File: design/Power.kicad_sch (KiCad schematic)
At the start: 48 parts, among them U2 TC2117, U3 DRV8302

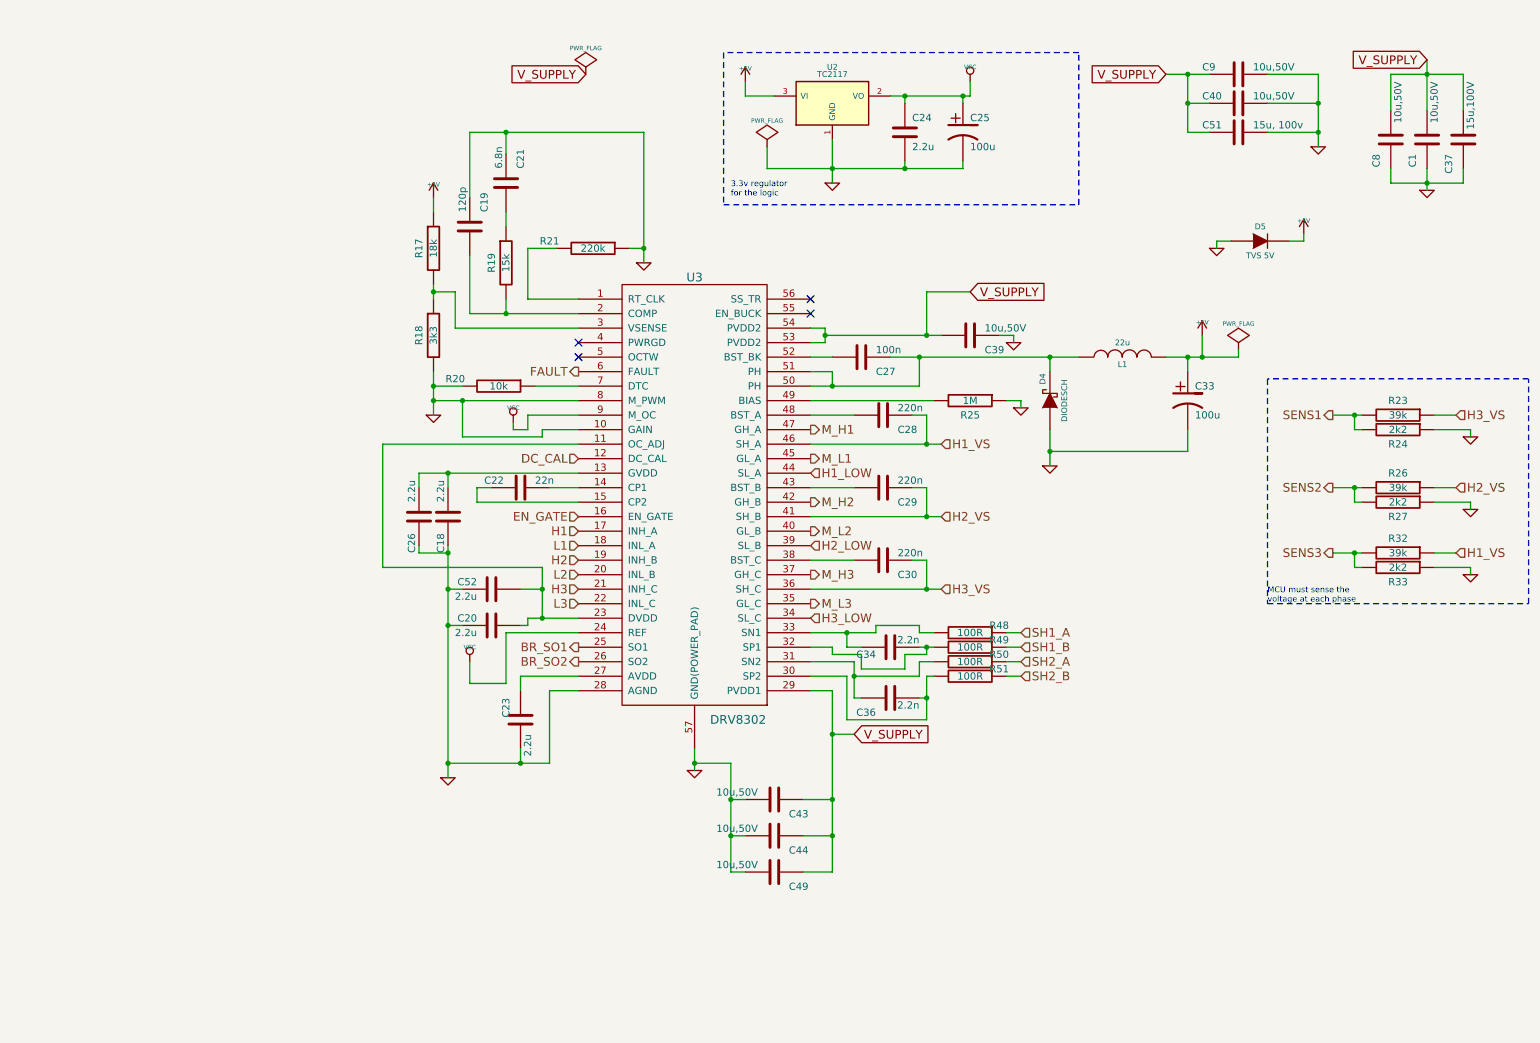
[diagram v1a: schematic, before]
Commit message: Actualización VESC6.4
Actualización a esquemáticos de VESC6.4, faltan asignación de huellas y descripción a cada elemento.
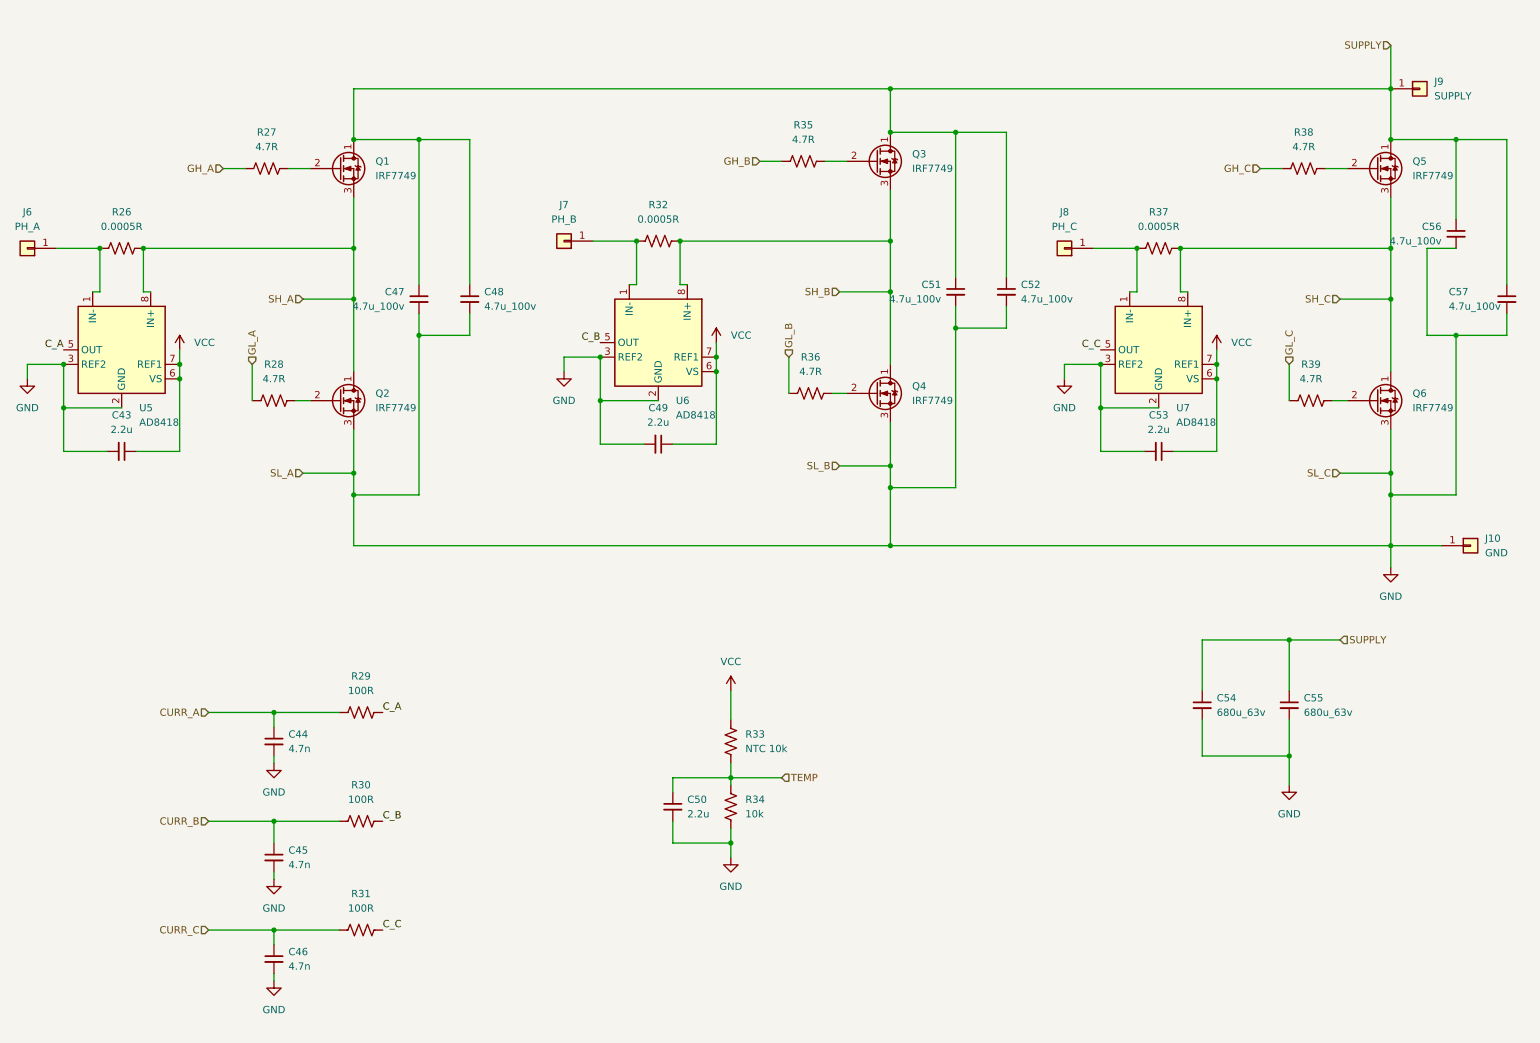
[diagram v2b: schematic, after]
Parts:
- removed C1, C39, C40, C43, C44, C49, C8, C9: 10u,50V, CRF1:SMD-1206, symbol BLDC_4-rescue1:C-RESCUE-BLDC_4
- removed C18, C20, C23, C24, C26, C52: 2.2u, CRF1:SMD-0603_c, symbol BLDC_4-rescue1:C-RESCUE-BLDC_4
- removed C19: 120p, CRF1:SMD-0603_c, symbol BLDC_4-rescue1:C-RESCUE-BLDC_4
- removed C21: 6.8n, CRF1:SMD-0603_c, symbol BLDC_4-rescue1:C-RESCUE-BLDC_4
- removed C22: 22n, CRF1:SMD-0603_c, symbol BLDC_4-rescue1:C-RESCUE-BLDC_4
- removed C25, C33: 100u, w_smd_cap:c_tant_B, symbol BLDC_4-rescue1:CP1-RESCUE-BLDC_4
- removed C27: 100n, CRF1:SMD-0603_c, symbol BLDC_4-rescue1:C-RESCUE-BLDC_4
- removed C28, C29, C30: 220n, CRF1:SMD-0603_c, symbol BLDC_4-rescue1:C-RESCUE-BLDC_4
- removed C34, C36: 2.2n, CRF1:SMD-0603_c, symbol BLDC_4-rescue1:C-RESCUE-BLDC_4
- removed C37: 15u,100V, w_smd_cap:c_2220, symbol BLDC_4-rescue1:C-RESCUE-BLDC_4
- removed C51: 15u, 100v, w_smd_cap:c_2220, symbol BLDC_4-rescue1:C-RESCUE-BLDC_4
- removed D4: DIODESCH, Diodes_SMD:SMA_Handsoldering, symbol BLDC_4-rescue1:DIODESCH
- removed D5: TVS 5V, w_smd_diode:do214ac, symbol BLDC_4-rescue1:DIODE
- removed L1: 22u, w_smd_inductors:inductor_smd_8x5mm, symbol BLDC_4-rescue1:INDUCTOR
- removed R17: 18k, CRF1:SMD-0603_r, symbol BLDC_4-rescue1:R-RESCUE-BLDC_4
- removed R18: 3k3, CRF1:SMD-0603_r, symbol BLDC_4-rescue1:R-RESCUE-BLDC_4
- removed R19: 15k, CRF1:SMD-0603_r, symbol BLDC_4-rescue1:R-RESCUE-BLDC_4
- removed R20: 10k, CRF1:SMD-0603_r, symbol BLDC_4-rescue1:R-RESCUE-BLDC_4
- removed R21: 220k, CRF1:SMD-0603_r, symbol BLDC_4-rescue1:R-RESCUE-BLDC_4
- removed R23, R26, R32: 39k, CRF1:SMD-0603_r, symbol BLDC_4-rescue1:R-RESCUE-BLDC_4
- removed R24, R27, R33: 2k2, CRF1:SMD-0603_r, symbol BLDC_4-rescue1:R-RESCUE-BLDC_4
- removed R25: 1M, CRF1:SMD-0603_r, symbol BLDC_4-rescue1:R-RESCUE-BLDC_4
- removed R48, R49, R50, R51: 100R, CRF1:SMD-0603_r, symbol BLDC_4-rescue1:R-RESCUE-BLDC_4
- removed U2: TC2117, CRF1:SOT-223, symbol BLDC_4-rescue1:NCP1117ST33T3G
- removed U3: DRV8302, CRF1:TSSOP-56-PP, symbol crf_11:DRV8302
- added C43, C49, C50, C53: 2.2u, Capacitor_SMD:C_0603_1608Metric, symbol Device:C_Small
- added C44, C45, C46: 4.7n, Capacitor_SMD:C_0603_1608Metric, symbol Device:C_Small
- added C47, C48, C51, C52, C56, C57: 4.7u_100v, Capacitor_SMD:C_0603_1608Metric, symbol Device:C_Small
- added C54, C55: 680u_63v, Capacitor_SMD:C_0603_1608Metric, symbol Device:C_Small
- added J10: GND, symbol Connector_Generic:Conn_01x01
- added J6: PH_A, symbol Connector_Generic:Conn_01x01
- added J7: PH_B, symbol Connector_Generic:Conn_01x01
- added J8: PH_C, symbol Connector_Generic:Conn_01x01
- added J9: SUPPLY, symbol Connector_Generic:Conn_01x01
- added Q1, Q2, Q3, Q4, Q5, Q6: IRF7749, Package_DirectFET:DirectFET_L8, symbol bldc:IRF7749L1PBF
- added R26, R32, R37: 0.0005R, Resistor_SMD:R_0603_1608Metric, symbol Device:R_US
- added R27, R28, R35, R36, R38, R39: 4.7R, Resistor_SMD:R_0603_1608Metric, symbol Device:R_US
- added R29, R30, R31: 100R, Resistor_SMD:R_0603_1608Metric, symbol Device:R_US
- added R33: NTC 10k, Resistor_SMD:R_0603_1608Metric, symbol Device:R_US
- added R34: 10k, Resistor_SMD:R_0603_1608Metric, symbol Device:R_US
- added U5, U6, U7: AD8418, symbol Amplifier_Current:AD8418
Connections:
- net GND: now also C43.2, C44.2, C45.2, C46.2, C47.2, C48.2, C49.2, C50.2, C51.2, C52.2, C53.2, C54.2, C55.2, C56.2, C57.2, J10.1 (Pin_1), Q2.3 (S), Q4.3 (S), Q6.3 (S), R34.2, U5.2 (GND), U5.3 (REF2), U6.2 (GND), U6.3 (REF2), U7.2 (GND), U7.3 (REF2)
- net VCC: now also C43.1, C49.1, C53.1, R33.1, U5.6 (VS), U5.7 (REF1), U6.6 (VS), U6.7 (REF1), U7.6 (VS), U7.7 (REF1)
- new net: Q3.2 (G), R35.1
- new net: J7.1 (Pin_1), R32.2, U6.1 (IN-)
- new net: Q4.2 (G), R36.1
- new net: J6.1 (Pin_1), R26.2, U5.1 (IN-)
- new net: Q1.2 (G), R27.1
- new net: Q2.2 (G), R28.1
- new net: J8.1 (Pin_1), R37.2, U7.1 (IN-)
- new net: Q5.2 (G), R38.1
- new net: Q6.2 (G), R39.1
- new net CURR_A: C44.1, R29.2
- new net CURR_B: C45.1, R30.2
- new net CURR_C: C46.1, R31.2
- new net C_A: R29.1, U5.5 (OUT)
- new net C_B: R30.1, U6.5 (OUT)
- new net C_C: R31.1, U7.5 (OUT)
- new net GH_A: R27.2
- new net GH_B: R35.2
- new net GH_C: R38.2
- new net GL_A: R28.2
- new net GL_B: R36.2
- new net GL_C: R39.2
- new net SH_A: Q1.3 (S), Q2.1 (D), R26.1, U5.8 (IN+)
- new net SH_B: Q3.3 (S), Q4.1 (D), R32.1, U6.8 (IN+)
- new net SH_C: Q5.3 (S), Q6.1 (D), R37.1, U7.8 (IN+)
- new net SUPPLY: C47.1, C48.1, C51.1, C52.1, C54.1, C55.1, C56.1, C57.1, J9.1 (Pin_1), Q1.1 (D), Q3.1 (D), Q5.1 (D)
- new net TEMP: C50.1, R33.2, R34.1
- no-connect marks 4 -> 0
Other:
- note removed: "3.3v regulator for the logic"
- note removed: "MCU must sense the voltage at each phase"
- company: Benjamin Vedder -> UTN
- title: BLDC Driver 4.11 -> bldc-controller-edp

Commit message: Impresión de esquemático en pdf
Impresión de la versión del esquemático en la carpeta /pdf
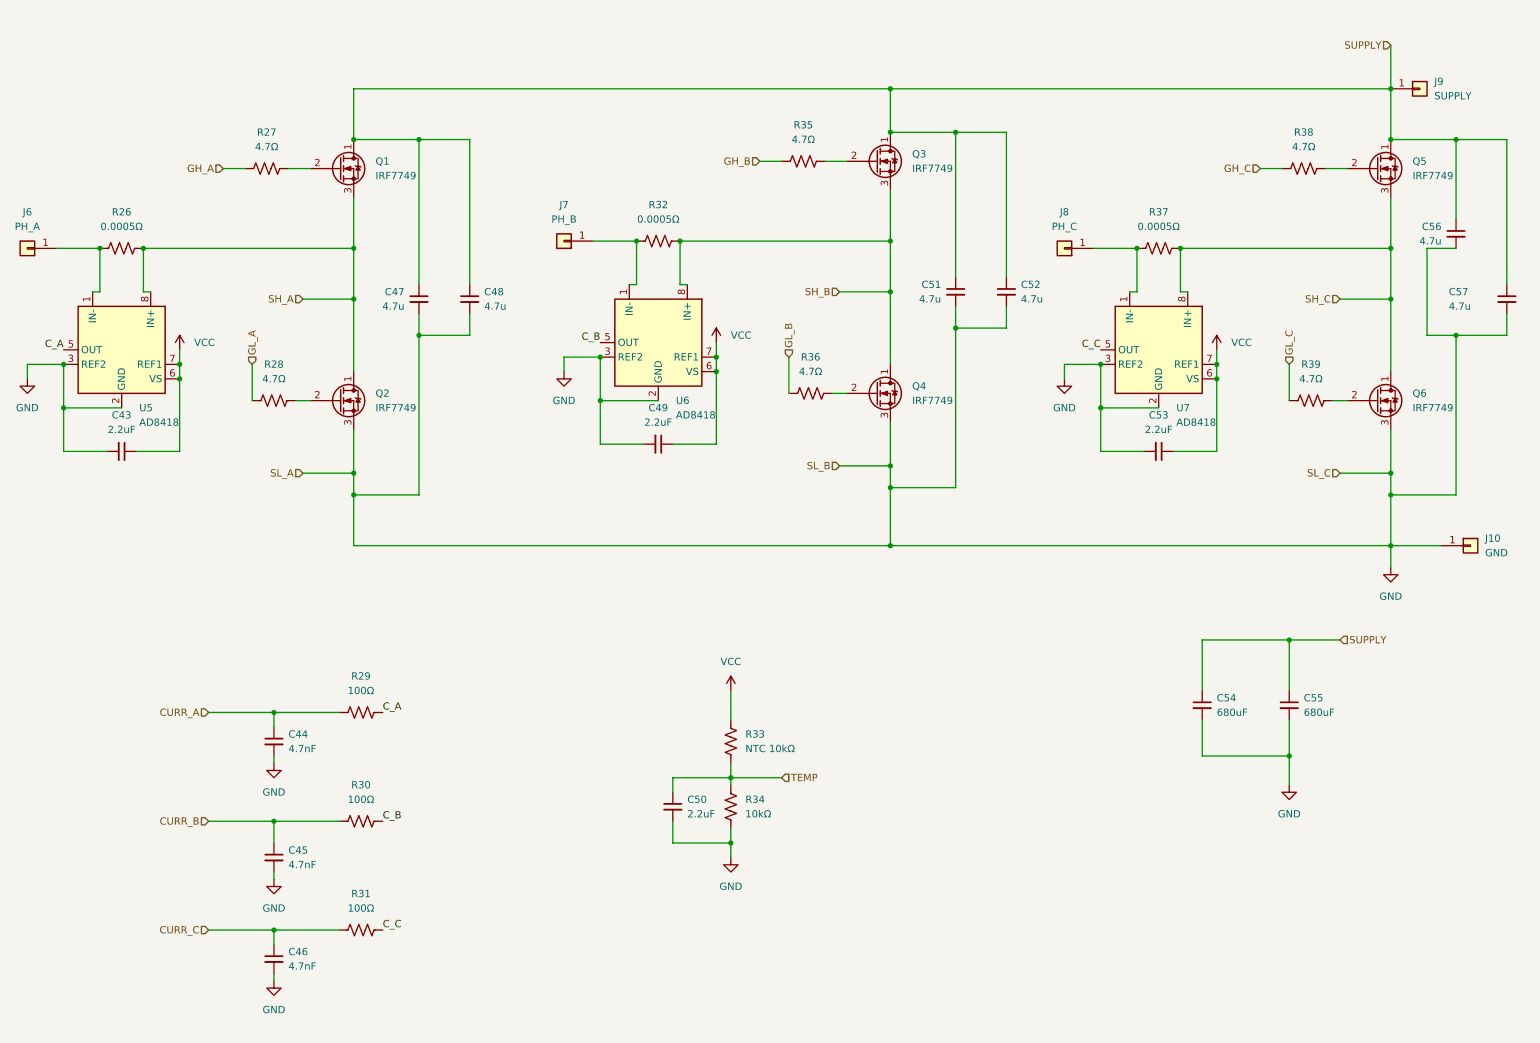
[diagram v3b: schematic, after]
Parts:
- C43, C49, C50, C53: value 2.2u -> 2.2uF
- C44, C45, C46: value 4.7n -> 4.7nF
- C47, C48, C51, C52, C56, C57: value 4.7u_100v -> 4.7u; footprint Capacitor_SMD:C_0603_1608Metric -> Capacitor_SMD:C_1210_3225Metric
- C54, C55: value 680u_63v -> 680uF; footprint Capacitor_SMD:C_0603_1608Metric -> Capacitor_THT:CP_Radial_D6.3mm_P2.50mm
- R26, R32, R37: value 0.0005R -> 0.0005Ω
- R27, R28, R35, R36, R38, R39: value 4.7R -> 4.7Ω
- R29, R30, R31: value 100R -> 100Ω
- R33: value NTC 10k -> NTC 10kΩ
- R34: value 10k -> 10kΩ
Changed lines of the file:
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@@
 			)
 		)
-		(property "Value" "4.7R"
+		(property "Value" "4.7Ω"
 			(at 154.94 36.83 90)
 			(effects
@@
 			)
 		)
-		(property "Value" "0.0005R"
+		(property "Value" "0.0005Ω"
 			(at 129.54 50.8 90)
 			(effects
@@
 			)
 		)
-		(property "Value" "4.7R"
+		(property "Value" "4.7Ω"
 			(at 156.21 77.47 90)
 			(effects
@@
 			)
 		)
-		(property "Value" "4.7u_100v"
+		(property "Value" "4.7u"
 			(at 179.07 64.7762 0)
 			(effects
@@
 			)
 		)
-		(property "Footprint" "Capacitor_SMD:C_0603_1608Metric"
+		(property "Footprint" "Capacitor_SMD:C_1210_3225Metric"
 			(at 181.61 63.5 0)
 			(effects
@@
 			)
 		)
-		(property "Description" ""
+		(property "Description" "CAP CER 4.7UF 100V X7R 1210"
 			(at 181.61 63.5 0)
 			(effects
@@
 			)
 		)
-		(property "Value" "4.7u_100v"
+		(property "Value" "4.7u"
 			(at 193.04 64.7762 0)
 			(effects
@@
 			)
 		)
-		(property "Footprint" "Capacitor_SMD:C_0603_1608Metric"
+		(property "Footprint" "Capacitor_SMD:C_1210_3225Metric"
 			(at 190.5 63.5 0)
 			(effects
@@
 			)
 		)
-		(property "Description" ""
+		(property "Description" "CAP CER 4.7UF 100V X7R 1210"
 			(at 190.5 63.5 0)
 			(effects
@@
 			)
 		)
-		(property "Value" "2.2u"
+		(property "Value" "2.2uF"
 			(at 129.5336 86.36 90)
 			(effects
@@
 			)
 		)
-		(property "Value" "4.7R"
+		(property "Value" "4.7Ω"
 			(at 60.96 38.1 90)
 			(effects
@@
 			)
 		)
-		(property "Value" "0.0005R"
+		(property "Value" "0.0005Ω"
 			(at 35.56 52.07 90)
 			(effects
@@
 			)
 		)
-		(property "Value" "4.7R"
+		(property "Value" "4.7Ω"
 			(at 62.23 78.74 90)
 			(effects
@@
 			)
 		)
-		(property "Value" "4.7u_100v"
+		(property "Value" "4.7u"
 			(at 85.09 66.0462 0)
 			(effects
@@
 			)
 		)
-		(property "Footprint" "Capacitor_SMD:C_0603_1608Metric"
+		(property "Footprint" "Capacitor_SMD:C_1210_3225Metric"
 			(at 87.63 64.77 0)
 			(effects
@@
 			)
 		)
-		(property "Description" ""
+		(property "Description" "CAP CER 4.7UF 100V X7R 1210"
 			(at 87.63 64.77 0)
 			(effects
@@
 			)
 		)
-		(property "Value" "4.7u_100v"
+		(property "Value" "4.7u"
 			(at 99.06 66.0462 0)
 			(effects
@@
 			)
 		)
-		(property "Footprint" "Capacitor_SMD:C_0603_1608Metric"
+		(property "Footprint" "Capacitor_SMD:C_1210_3225Metric"
 			(at 96.52 64.77 0)
 			(effects
@@
 			)
 		)
-		(property "Description" ""
+		(property "Description" "CAP CER 4.7UF 100V X7R 1210"
 			(at 96.52 64.77 0)
 			(effects
@@
 			)
 		)
-		(property "Value" "2.2u"
+		(property "Value" "2.2uF"
 			(at 35.5536 87.63 90)
 			(effects
@@
 			)
 		)
-		(property "Value" "4.7R"
+		(property "Value" "4.7Ω"
 			(at 242.57 38.1 90)
 			(effects
@@
 			)
 		)
-		(property "Value" "0.0005R"
+		(property "Value" "0.0005Ω"
 			(at 217.17 52.07 90)
 			(effects
@@
 			)
 		)
-		(property "Value" "4.7R"
+		(property "Value" "4.7Ω"
 			(at 243.84 78.74 90)
 			(effects
@@
 			)
 		)
-		(property "Value" "4.7u_100v"
+		(property "Value" "4.7u"
 			(at 266.7 54.6162 0)
 			(effects
@@
 			)
 		)
-		(property "Footprint" "Capacitor_SMD:C_0603_1608Metric"
+		(property "Footprint" "Capacitor_SMD:C_1210_3225Metric"
 			(at 269.24 53.34 0)
 			(effects
@@
 			)
 		)
-		(property "Description" ""
+		(property "Description" "CAP CER 4.7UF 100V X7R 1210"
 			(at 269.24 53.34 0)
 			(effects
@@
 			)
 		)
-		(property "Value" "4.7u_100v"
+		(property "Value" "4.7u"
 			(at 267.97 66.04 0)
 			(effects
@@
 			)
 		)
-		(property "Footprint" "Capacitor_SMD:C_0603_1608Metric"
+		(property "Footprint" "Capacitor_SMD:C_1210_3225Metric"
 			(at 278.13 64.77 0)
 			(effects
@@
 			)
 		)
-		(property "Description" ""
+		(property "Description" "CAP CER 4.7UF 100V X7R 1210"
 			(at 278.13 64.77 0)
 			(effects
@@
 			)
 		)
-		(property "Value" "2.2u"
+		(property "Value" "2.2uF"
 			(at 217.1636 87.63 90)
 			(effects
@@
 			)
 		)
-		(property "Value" "100R"
+		(property "Value" "100Ω"
 			(at 77.47 133.35 90)
 			(effects
@@
 			)
 		)
-		(property "Value" "100R"
+		(property "Value" "100Ω"
 			(at 77.47 152.4 90)
 			(effects
@@
 			)
 		)
-		(property "Value" "100R"
+		(property "Value" "100Ω"
 			(at 77.47 171.45 90)
 			(effects
@@
 			)
 		)
-		(property "Value" "4.7n"
+		(property "Value" "4.7nF"
 			(at 64.77 143.5162 0)
 			(effects
@@
 			)
 		)
-		(property "Description" ""
+		(property "Description" "CAP CER 0603 4.7NF 16V X7R 10%"
 			(at 62.23 142.24 0)
 			(effects
@@
 			)
 		)
-		(property "Value" "4.7n"
+		(property "Value" "4.7nF"
 			(at 64.77 163.8362 0)
 			(effects
@@
 			)
 		)
-		(property "Description" ""
+		(property "Description" "CAP CER 0603 4.7NF 16V X7R 10%"
 			(at 62.23 162.56 0)
 			(effects
@@
 			)
 		)
-		(property "Value" "4.7n"
+		(property "Value" "4.7nF"
 			(at 64.77 181.6162 0)
 			(effects
@@
 			)
 		)
-		(property "Description" ""
+		(property "Description" "CAP CER 0603 4.7NF 16V X7R 10%"
 			(at 62.23 180.34 0)
 			(effects
@@
 			)
 		)
-		(property "Value" "10k"
+		(property "Value" "10kΩ"
 			(at 144.78 154.9399 0)
 			(effects
@@
 			)
 		)
-		(property "Value" "NTC 10k"
+		(property "Value" "NTC 10kΩ"
 			(at 144.78 143.5099 0)
 			(effects
@@
 			)
 		)
-		(property "Value" "2.2u"
+		(property "Value" "2.2uF"
 			(at 134.62 154.9462 0)
 			(effects
@@
 			)
 		)
-		(property "Value" "680u_63v"
+		(property "Value" "680uF"
 			(at 227.33 137.1662 0)
 			(effects
@@
 			)
 		)
-		(property "Footprint" "Capacitor_SMD:C_0603_1608Metric"
+		(property "Footprint" "Capacitor_THT:CP_Radial_D6.3mm_P2.50mm"
 			(at 224.79 135.89 0)
 			(effects
@@
 			)
 		)
-		(property "Description" ""
+		(property "Description" "CAP ALUM 680UF 20% 80V"
 			(at 224.79 135.89 0)
 			(effects
@@
 			)
 		)
-		(property "Value" "680u_63v"
+		(property "Value" "680uF"
 			(at 242.57 137.1662 0)
 			(effects
@@
 			)
 		)
-		(property "Footprint" "Capacitor_SMD:C_0603_1608Metric"
+		(property "Footprint" "Capacitor_THT:CP_Radial_D6.3mm_P2.50mm"
 			(at 240.03 135.89 0)
 			(effects
@@
 			)
 		)
-		(property "Description" ""
+		(property "Description" "CAP ALUM 680UF 20% 80V"
 			(at 240.03 135.89 0)
 			(effects
